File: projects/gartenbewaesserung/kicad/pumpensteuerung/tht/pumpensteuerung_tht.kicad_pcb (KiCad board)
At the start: 2 copper layers, 100 x 85 mm, 26 parts, among them J1 Screw_Terminal_01x03, J2 Screw_Terminal_01x02, J3 I2C Terminal, J4 Screw_Terminal_01x03, J5 Screw_Terminal_01x03, K2 SANYOU_SRD_Form_C, K3 SANYOU_SRD_Form_C, K4 SANYOU_SRD_Form_C, Q1 S8050, Q2 S8050, Q3 S8050

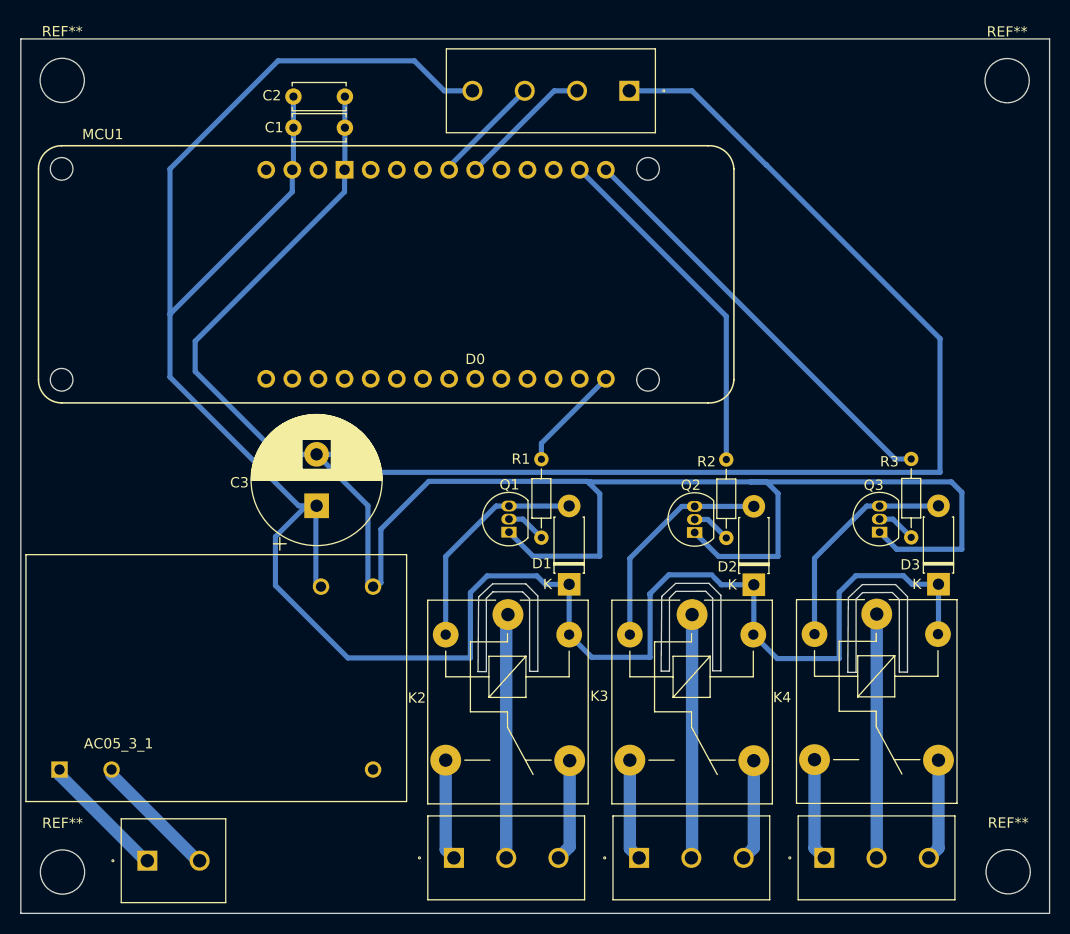
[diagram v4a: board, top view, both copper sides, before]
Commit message: [gartenbewaesserung(pcb)] move power supply a litle bit
move the power supply a little bit more into the center, so we have more
clearance in the case.
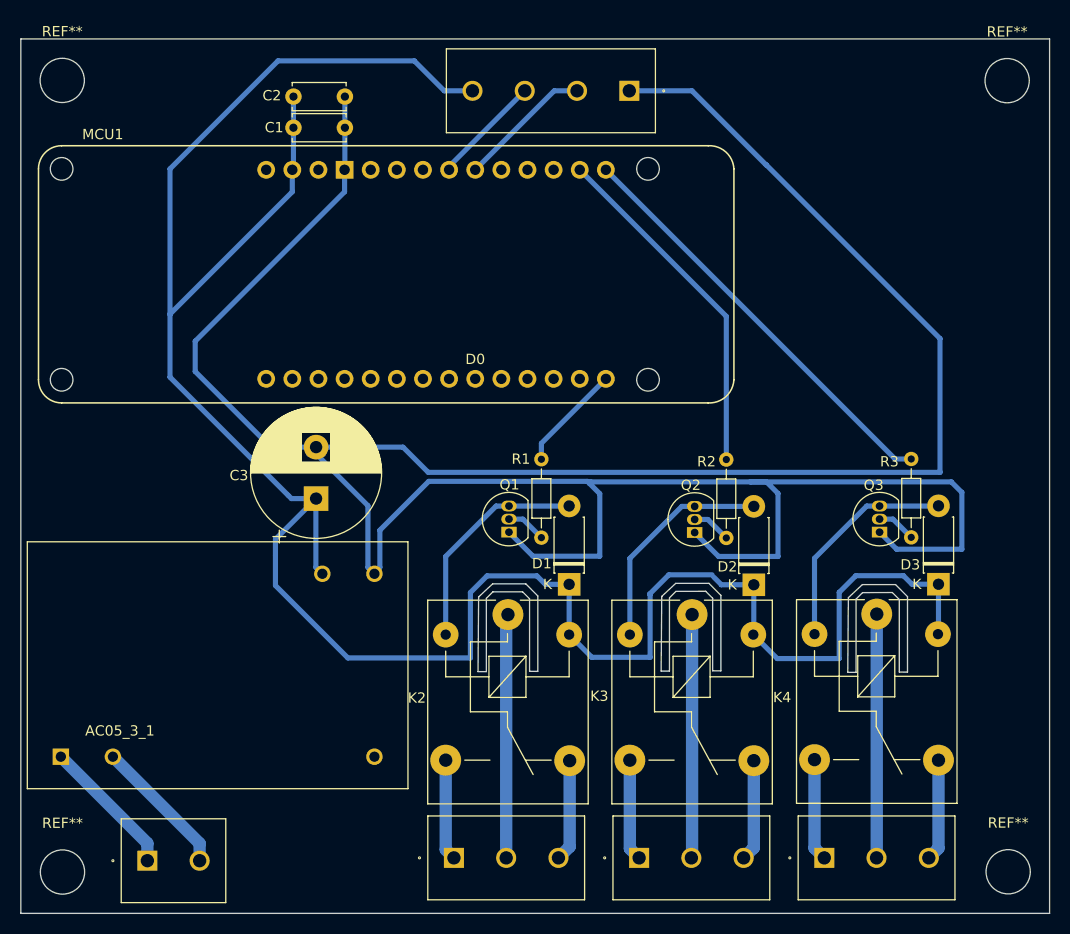
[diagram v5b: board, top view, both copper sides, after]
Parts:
- moved AC05_3_1 1.26 mm to (69.6, 109.9)
- moved C3 0.70 mm to (79.2, 93.7)
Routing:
- net GND: track 12.5 -> 14.0 mm
- net VCC: track 12.5 -> 14.0 mm
